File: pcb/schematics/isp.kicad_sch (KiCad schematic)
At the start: 35 parts

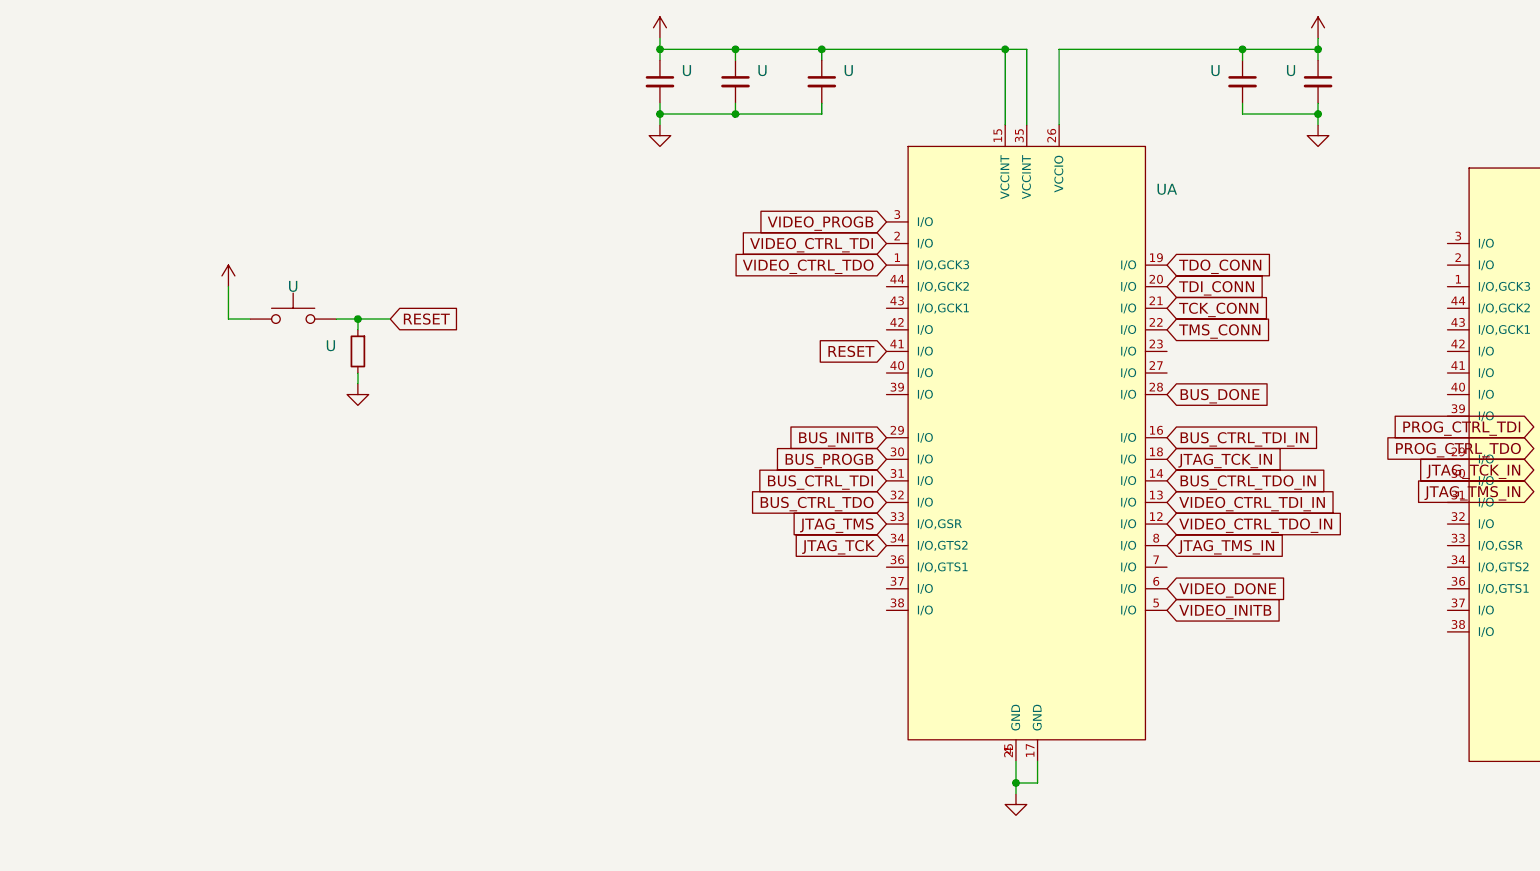
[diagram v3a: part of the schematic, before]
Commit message: add status led in the programming interface schematic
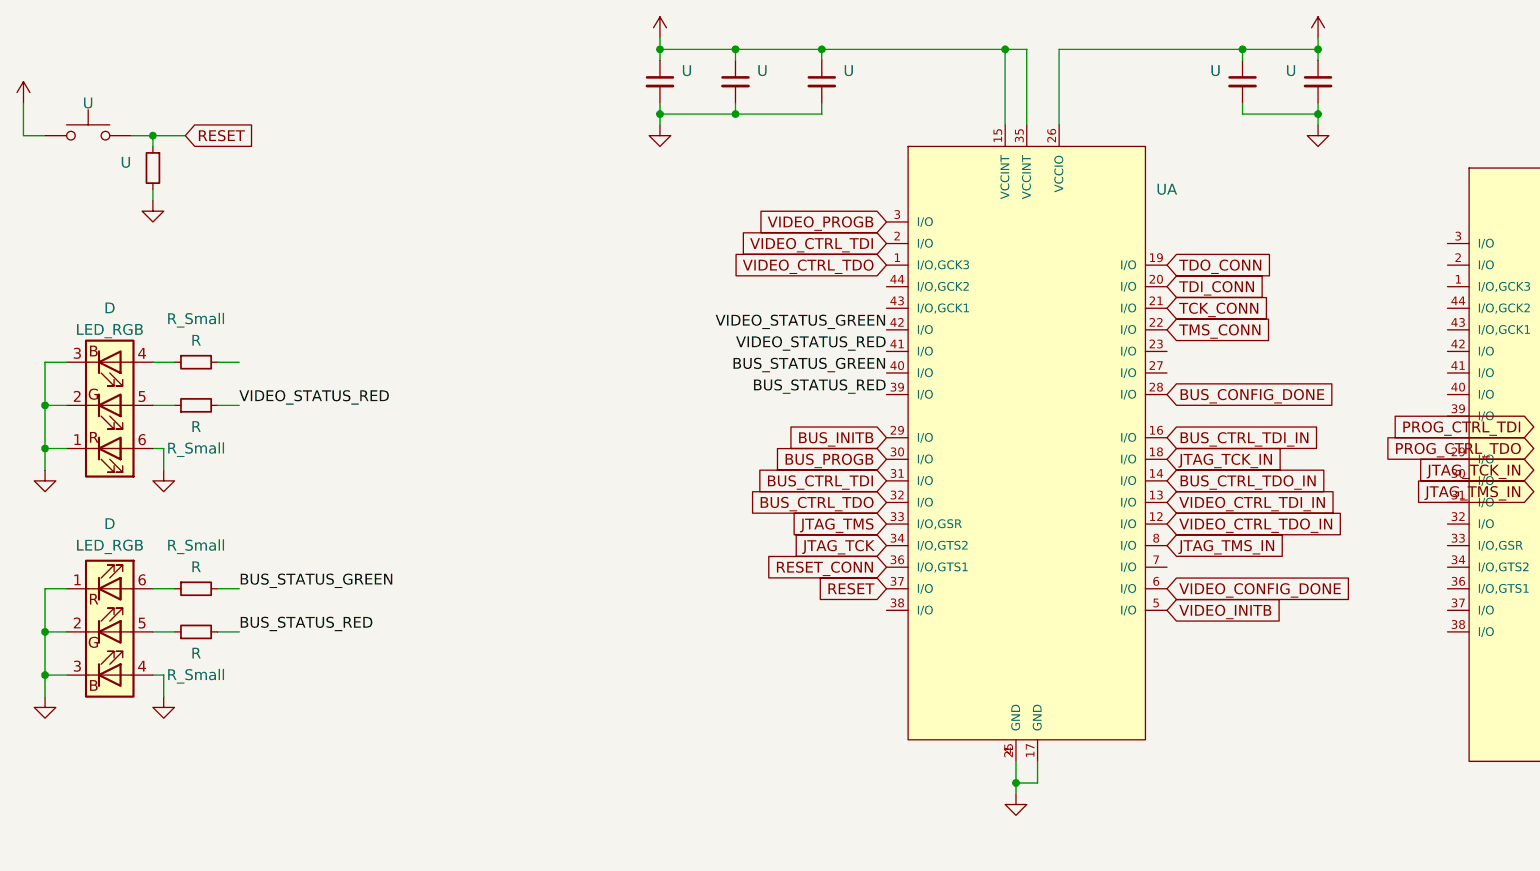
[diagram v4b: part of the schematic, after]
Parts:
- added D (x2): LED_RGB, symbol Device:LED_RGB
- added R (x4): R_Small, symbol Device:R_Small
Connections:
- net GND: now also D.1 (RK), D.1 (RK), D.2 (GK), D.2 (GK), D.3 (BK), D.3 (BK), D.4 (BA), D.6 (RA)
- net RESET: now also U.37 (I/O); no longer U.41 (I/O)
- net RESET_CONN: now reaches U.36 (I/O,GTS1)
- net BUS_STATUS_RED: now reaches U.39 (I/O)
- net BUS_STATUS_RED: now also R.2
- net BUS_STATUS_GREEN: now reaches U.40 (I/O)
- net BUS_STATUS_GREEN: now also R.2
- net VIDEO_STATUS_GREEN: now reaches U.42 (I/O)
- net BUS_DONE renamed BUS_CONFIG_DONE
- net VIDEO_DONE renamed VIDEO_CONFIG_DONE
- new net: D.6 (RA), R.1
- new net: D.4 (BA), R.1
- new net: D.5 (GA), R.1 (x2)
- new net VIDEO_STATUS_RED: R.2, U.41 (I/O)
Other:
- moved on the sheet: U

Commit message: add rgb led status
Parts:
- D: Part Number (none) -> CLX6F-FKC-CNP1ST1E1BB7D3D3
- R: Part Number (none) -> CR0603-FX-60R4ELF
- R: Part Number (none) -> ERJ-3EKF80R6V

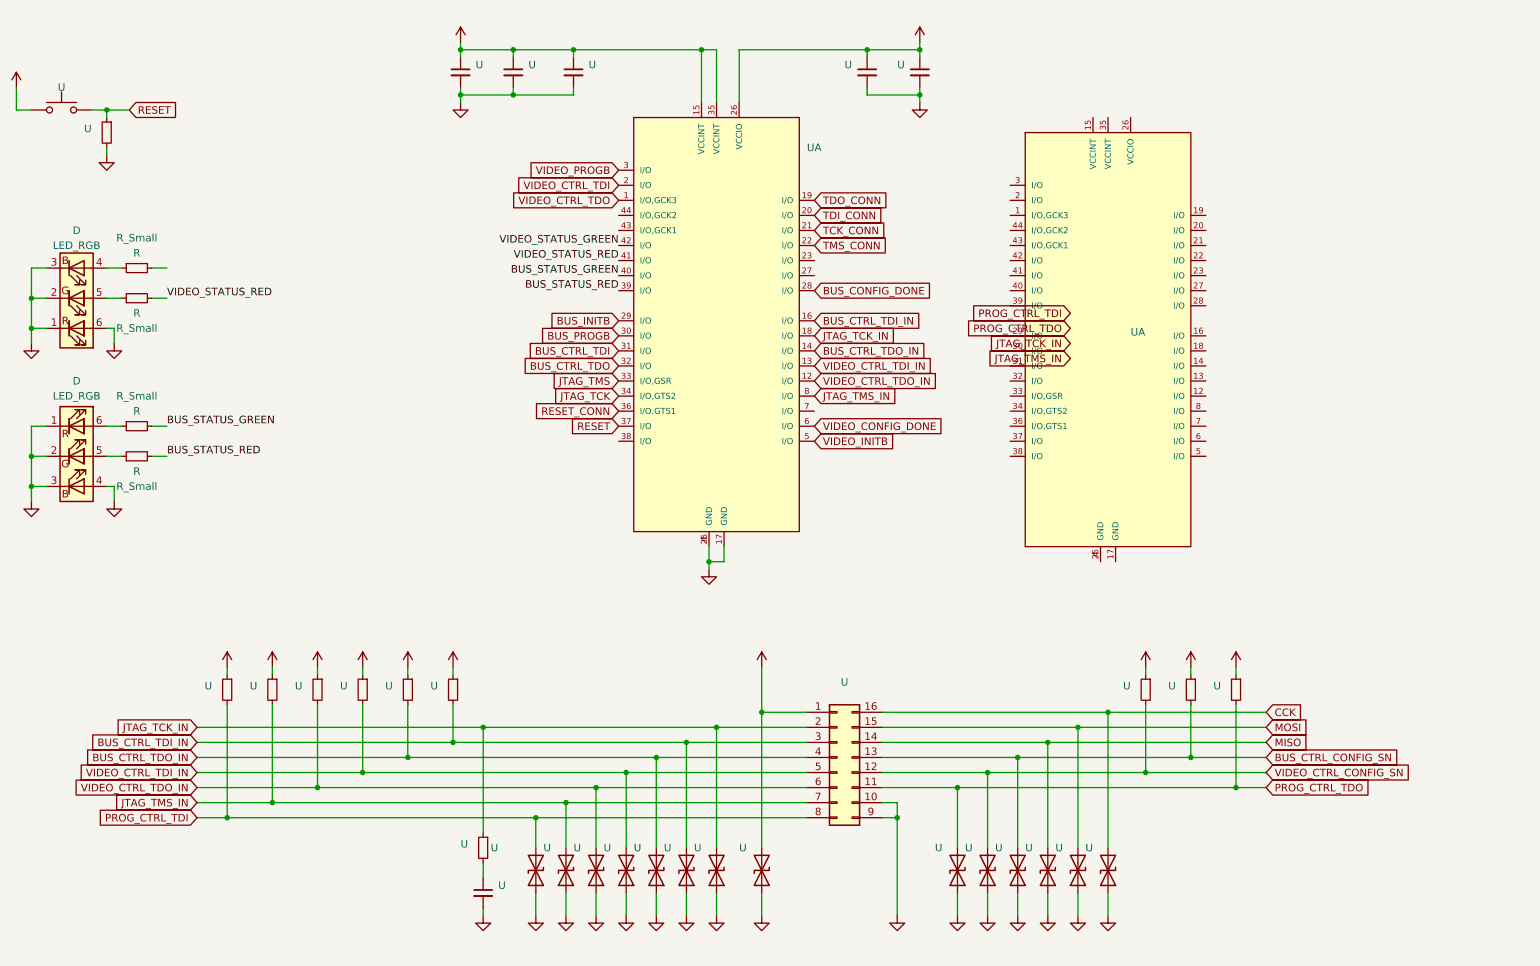
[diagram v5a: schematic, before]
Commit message: add status leds and jtag chain jumpers
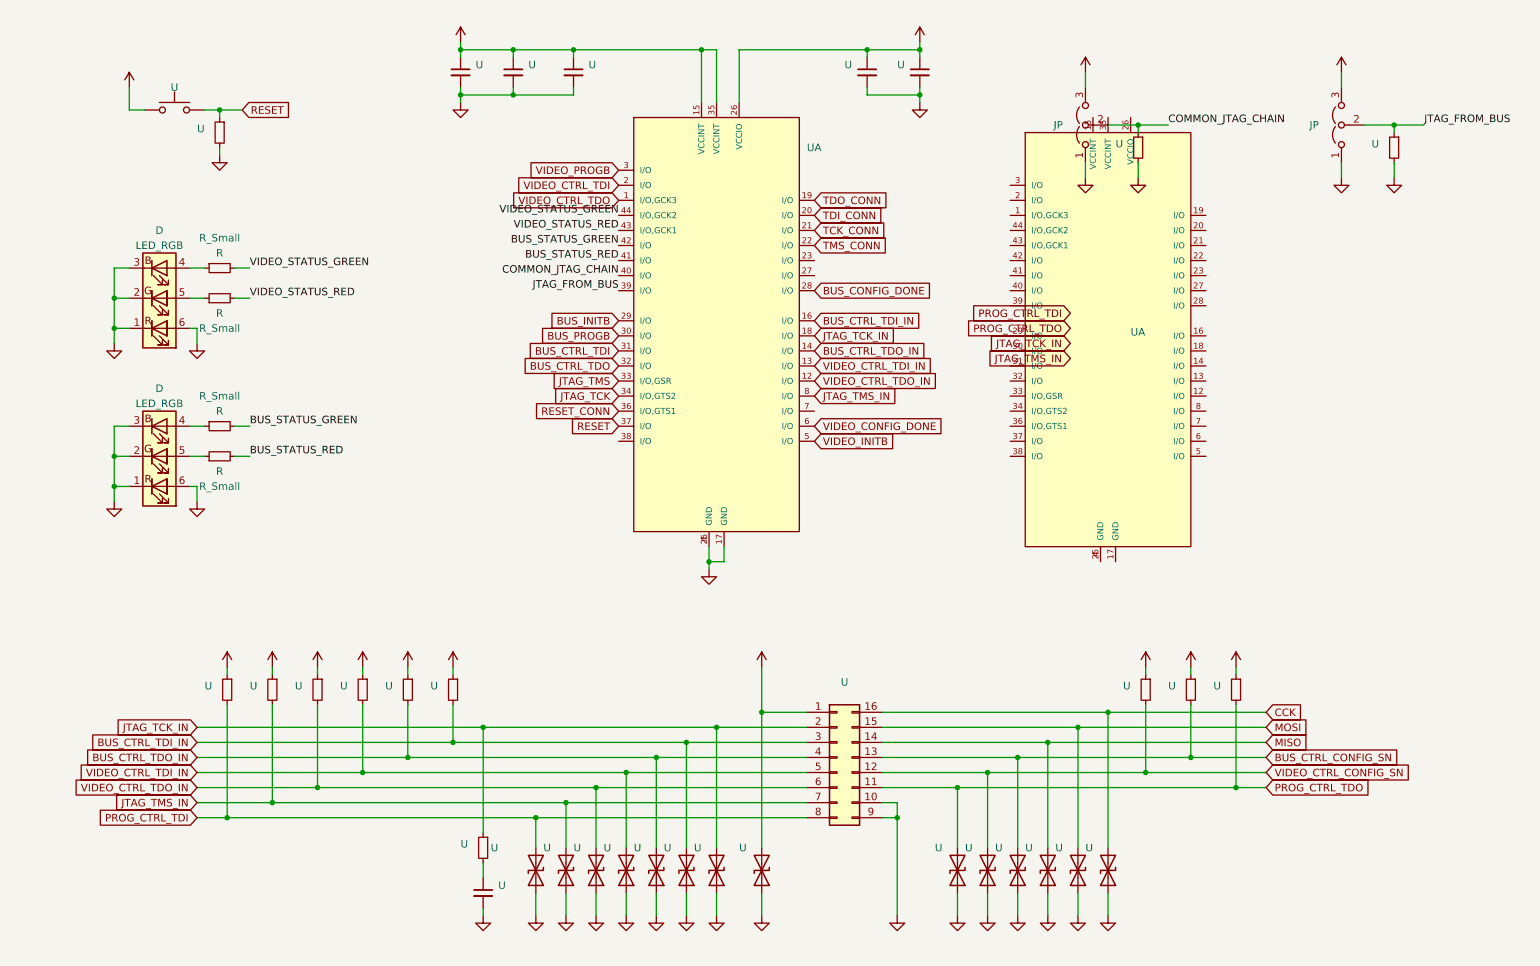
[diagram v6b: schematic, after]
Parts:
- added JP (x2): Jumper_3_Open, symbol Jumper:Jumper_3_Open
- added U (x2): (no value), symbol Device:R_Small
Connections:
- net +3V3: now also JP.3 (B), JP.3 (B)
- net BUS_STATUS_GREEN: now also U.42 (I/O); no longer U.40 (I/O)
- net BUS_STATUS_RED: now also U.41 (I/O); no longer U.39 (I/O)
- net GND: now also D.6 (RA), JP.1 (A), JP.1 (A), U.2, U.2; no longer D.4 (BA)
- net VIDEO_STATUS_GREEN: now also R.2, U.44 (I/O,GCK2); no longer U.42 (I/O)
- net VIDEO_STATUS_RED: now also U.43 (I/O,GCK1); no longer U.41 (I/O)
- net at R.1: now also D.4 (BA); no longer D.6 (RA)
- new net COMMON_JTAG_CHAIN: JP.2 (C), U.1, U.40 (I/O)
- new net JTAG_FROM_BUS: JP.2 (C), U.1, U.39 (I/O)
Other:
- moved on the sheet: D, R, U

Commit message: passed erc and drc
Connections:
- no-connect marks 0 -> 4
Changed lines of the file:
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@@
   (junction (at 142.24 138.43) (diameter 0) (color 0 0 0 0)
   )
+  (no_connect (at 130.81 87.63))
+  (no_connect (at 163.83 57.15))
+  (no_connect (at 163.83 59.69))
+  (no_connect (at 163.83 82.55))
   (wire (pts (xy 64.77 132.08) (xy 64.77 151.13))
     (stroke (width 0) (type default))
